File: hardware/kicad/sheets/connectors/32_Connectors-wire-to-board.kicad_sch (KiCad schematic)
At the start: 14 parts, among them CN12 DB142R-5_08-8P

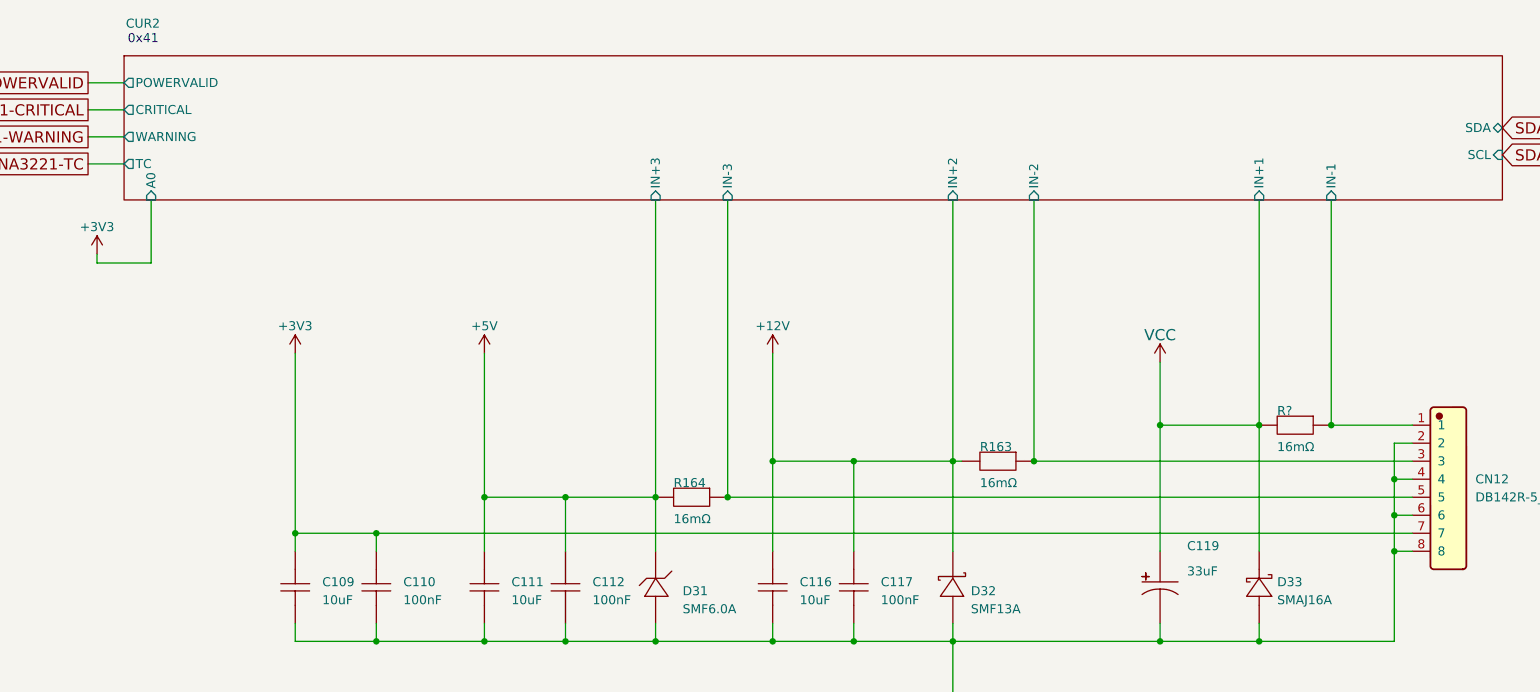
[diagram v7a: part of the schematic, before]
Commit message: more sheet simplfiication and pre simpler 12v sym
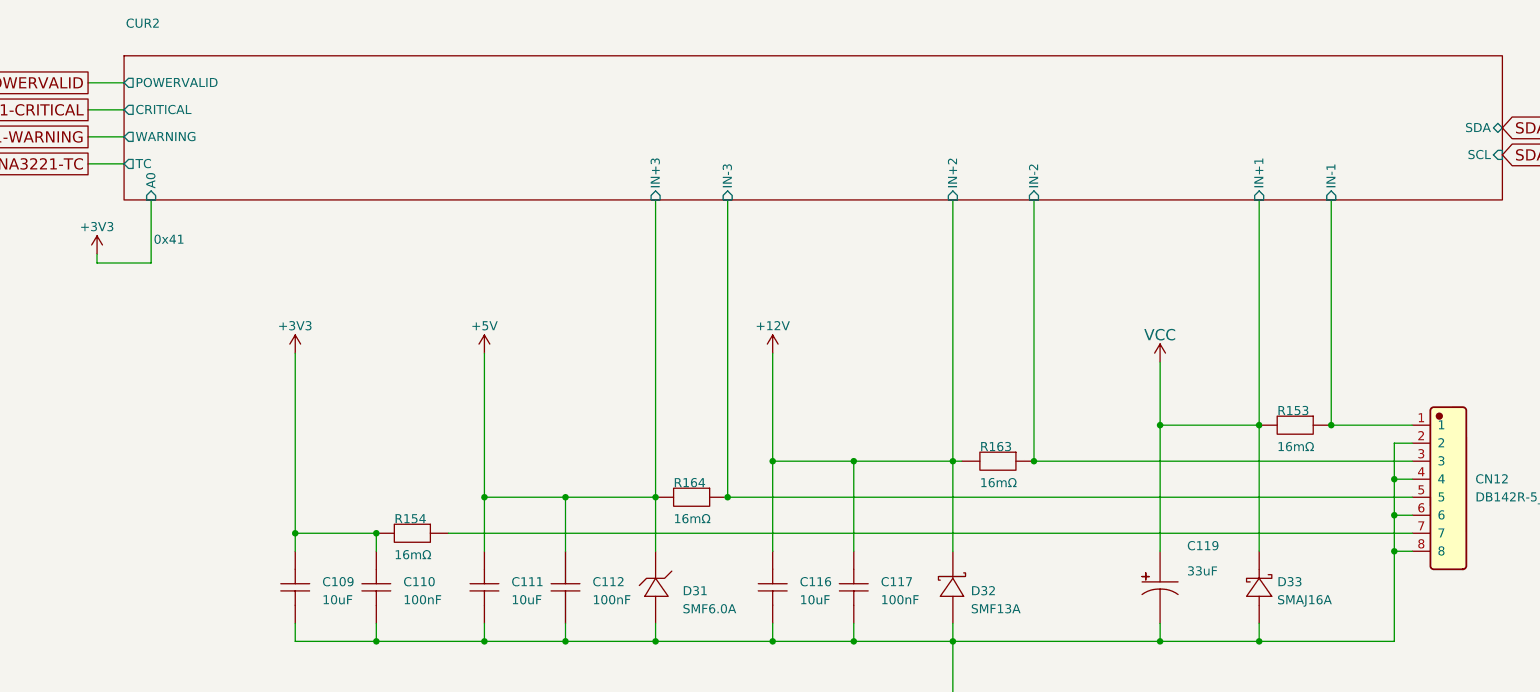
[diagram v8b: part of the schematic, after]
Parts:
- added R154: 16mΩ, Resistor_SMD:R_2512_6332Metric, symbol 5v rail sm-easyedapro:LR123WF160MT4E
- gave numbers to parts that had none: 1
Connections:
- net +3V3: now also R154.2; no longer CN12.7
- new net: CN12.7, R154.1
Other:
- note removed: "0x41"
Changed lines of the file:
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@@
 		(date "2026-02-16")
-	)
-	(text "0x41"
-		(exclude_from_sim no)
-		(at 74.168 23.876 0)
-		(effects
-			(font
-				(size 1.27 1.27)
-			)
-			(justify left bottom)
-		)
 	)
 	(junction
@@
 	(wire
 		(pts
+			(xy 119.38 92.71) (xy 255.27 92.71)
+		)
+		(stroke
+			(width 0)
+			(type default)
+		)
+	)
+	(wire
+		(pts
 			(xy 243.84 45.72) (xy 243.84 77.47)
 		)
@@
 		(pts
 			(xy 97.79 92.71) (xy 109.22 92.71)
-		)
-		(stroke
-			(width 0)
-			(type default)
-		)
-	)
-	(wire
-		(pts
-			(xy 109.22 92.71) (xy 255.27 92.71)
 		)
 		(stroke
@@
 	)
 	(symbol
+		(lib_id "5v rail sm-easyedapro:LR123WF160MT4E")
+		(at 114.3 92.71 0)
+		(mirror y)
+		(unit 1)
+		(exclude_from_sim no)
+		(in_bom yes)
+		(on_board yes)
+		(dnp no)
+		(property "Reference" "R154"
+			(at 111.76 91.44 0)
+			(effects
+				(font
+					(size 1.27 1.27)
+				)
+				(justify right bottom)
+			)
+		)
+		(property "Value" "16mΩ"
+			(at 111.76 96.52 0)
+			(effects
+				(font
+					(size 1.27 1.27)
+				)
+				(justify right bottom)
+			)
+		)
+		(property "Footprint" "Resistor_SMD:R_2512_6332Metric"
+			(at 114.3 92.71 0)
+			(effects
+				(font
+					(size 1.27 1.27)
+				)
+				(hide yes)
+			)
+		)
+		(property "Datasheet" ""
+			(at 114.3 92.71 0)
+			(effects
+				(font
+					(size 1.27 1.27)
+				)
+				(hide yes)
+			)
+		)
+		(property "Description" "Type:Current Sensing Resistors Resistance: Tolerance:±1% Tolerance:±1% Power(Watts): Temperature Coefficient:±50ppm/°C Temperature Coefficient:±50ppm/°C Mounting Type:Patch"
+			(at 114.3 92.71 0)
+			(effects
+				(font
+					(size 1.27 1.27)
+				)
+				(hide yes)
+			)
+		)
+		(property "Manufacturer Part" "LR123WF160MT4E"
+			(at 114.3 92.71 0)
+			(effects
+				(font
+					(size 1.27 1.27)
+				)
+				(hide yes)
+			)
+		)
+		(property "Manufacturer" "UNI-ROYAL(厚声)"
+			(at 114.3 92.71 0)
+			(effects
+				(font
+					(size 1.27 1.27)
+				)
+				(hide yes)
+			)
+		)
+		(property "Supplier Part" "C5775686"
+			(at 114.3 92.71 0)
+			(effects
+				(font
+					(size 1.27 1.27)
+				)
+				(hide yes)
+			)
+		)
+		(property "Supplier" "LCSC"
+			(at 114.3 92.71 0)
+			(effects
+				(font
+					(size 1.27 1.27)
+				)
+				(hide yes)
+			)
+		)
+		(property "LCSC Part Name" "16mΩ ±1% 3W"
+			(at 114.3 92.71 0)
+			(effects
+				(font
+					(size 1.27 1.27)
+				)
+				(hide yes)
+			)
+		)
+		(pin "1"
+		)
+		(pin "2"
+		)
+		(instances
+			(project "svea_powerboard_rev3"
+				(path "/3f85abf4-0b95-4c4a-b7e9-06f59ca1ea3d/5c2e021f-c2d4-49e2-8c36-9a64f1f12005/8d05c3b8-20a4-4a7f-9b20-01f8d5d5be51/d2f9c6a1-10e3-4d4e-9da8-c4d6204f6532"
+					(reference "R154")
+					(unit 1)
+				)
+			)
+		)
+	)
+	(symbol
 		(lib_id "JLCImport:DB142R-5_08-8P")
 		(at 260.35 86.36 0)
@@
 		(on_board yes)
 		(dnp no)
-		(property "Reference" "R?"
+		(property "Reference" "R153"
 			(at 236.22 76.2 0)
 			(effects
@@
 			(project "svea_powerboard_rev3"
 				(path "/3f85abf4-0b95-4c4a-b7e9-06f59ca1ea3d/5c2e021f-c2d4-49e2-8c36-9a64f1f12005/8d05c3b8-20a4-4a7f-9b20-01f8d5d5be51/d2f9c6a1-10e3-4d4e-9da8-c4d6204f6532"
-					(reference "R?")
+					(reference "R153")
 					(unit 1)
 				)
@@
 			)
 		)
+		(property "i2c Address" "0x41"
+			(at 80.01 51.308 0)
+			(effects
+				(font
+					(size 1.27 1.27)
+				)
+			)
+		)
